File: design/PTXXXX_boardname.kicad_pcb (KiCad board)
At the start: 2 copper layers, 0 parts

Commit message: place some dummy parts for 1.0 1A release
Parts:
- added REF**: CP_Elec_3x5.3, Capacitor_SMD:CP_Elec_3x5.3, F.Cu at (120.1, 79.5)
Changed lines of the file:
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@@
     (tracks 0)
     (zones 0)
-    (modules 0)
+    (modules 1)
     (nets 1)
   )
@@
     (uvia_drill 0.1)
   )
+  (module Capacitor_SMD:CP_Elec_3x5.3 (layer F.Cu)
+    (at 120.1 79.5)
+    (descr "SMT capacitor, aluminium electrolytic, 3x5.3, Cornell Dubilier Electronics ")
+    (tags "Capacitor Electrolytic")
+    (attr smd)
+    (fp_text reference REF** (at 0 -2.7) (layer F.SilkS)
+      (effects (font (size 1 1) (thickness 0.15)))
+    )
+    (fp_text value CP_Elec_3x5.3 (at 0 2.7) (layer F.Fab)
+      (effects (font (size 1 1) (thickness 0.15)))
+    )
+    (fp_text user %R (at 0 0) (layer F.Fab)
+      (effects (font (size 0.6 0.6) (thickness 0.09)))
+    )
+    (fp_line (start -2.85 1.05) (end -1.78 1.05) (layer F.CrtYd) (width 0.05))
+    (fp_line (start -2.85 -1.05) (end -2.85 1.05) (layer F.CrtYd) (width 0.05))
+    (fp_line (start -1.78 -1.05) (end -2.85 -1.05) (layer F.CrtYd) (width 0.05))
+    (fp_line (start -1.78 -1.05) (end -0.93 -1.9) (layer F.CrtYd) (width 0.05))
+    (fp_line (start -1.78 1.05) (end -0.93 1.9) (layer F.CrtYd) (width 0.05))
+    (fp_line (start -0.93 -1.9) (end 1.9 -1.9) (layer F.CrtYd) (width 0.05))
+    (fp_line (start -0.93 1.9) (end 1.9 1.9) (layer F.CrtYd) (width 0.05))
+    (fp_line (start 1.9 1.05) (end 1.9 1.9) (layer F.CrtYd) (width 0.05))
+    (fp_line (start 2.85 1.05) (end 1.9 1.05) (layer F.CrtYd) (width 0.05))
+    (fp_line (start 2.85 -1.05) (end 2.85 1.05) (layer F.CrtYd) (width 0.05))
+    (fp_line (start 1.9 -1.05) (end 2.85 -1.05) (layer F.CrtYd) (width 0.05))
+    (fp_line (start 1.9 -1.9) (end 1.9 -1.05) (layer F.CrtYd) (width 0.05))
+    (fp_line (start -2.1875 -1.6225) (end -2.1875 -1.2475) (layer F.SilkS) (width 0.12))
+    (fp_line (start -2.375 -1.435) (end -2 -1.435) (layer F.SilkS) (width 0.12))
+    (fp_line (start -1.570563 1.06) (end -0.870563 1.76) (layer F.SilkS) (width 0.12))
+    (fp_line (start -1.570563 -1.06) (end -0.870563 -1.76) (layer F.SilkS) (width 0.12))
+    (fp_line (start -0.870563 1.76) (end 1.76 1.76) (layer F.SilkS) (width 0.12))
+    (fp_line (start -0.870563 -1.76) (end 1.76 -1.76) (layer F.SilkS) (width 0.12))
+    (fp_line (start 1.76 -1.76) (end 1.76 -1.06) (layer F.SilkS) (width 0.12))
+    (fp_line (start 1.76 1.76) (end 1.76 1.06) (layer F.SilkS) (width 0.12))
+    (fp_line (start -0.960469 -0.95) (end -0.960469 -0.65) (layer F.Fab) (width 0.1))
+    (fp_line (start -1.110469 -0.8) (end -0.810469 -0.8) (layer F.Fab) (width 0.1))
+    (fp_line (start -1.65 0.825) (end -0.825 1.65) (layer F.Fab) (width 0.1))
+    (fp_line (start -1.65 -0.825) (end -0.825 -1.65) (layer F.Fab) (width 0.1))
+    (fp_line (start -1.65 -0.825) (end -1.65 0.825) (layer F.Fab) (width 0.1))
+    (fp_line (start -0.825 1.65) (end 1.65 1.65) (layer F.Fab) (width 0.1))
+    (fp_line (start -0.825 -1.65) (end 1.65 -1.65) (layer F.Fab) (width 0.1))
+    (fp_line (start 1.65 -1.65) (end 1.65 1.65) (layer F.Fab) (width 0.1))
+    (fp_circle (center 0 0) (end 1.5 0) (layer F.Fab) (width 0.1))
+    (pad 2 smd rect (at 1.5 0) (size 2.2 1.6) (layers F.Cu F.Paste F.Mask))
+    (pad 1 smd rect (at -1.5 0) (size 2.2 1.6) (layers F.Cu F.Paste F.Mask))
+    (model ${KISYS3DMOD}/Capacitor_SMD.3dshapes/CP_Elec_3x5.3.wrl
+      (at (xyz 0 0 0))
+      (scale (xyz 1 1 1))
+      (rotate (xyz 0 0 0))
+    )
+  )
 )

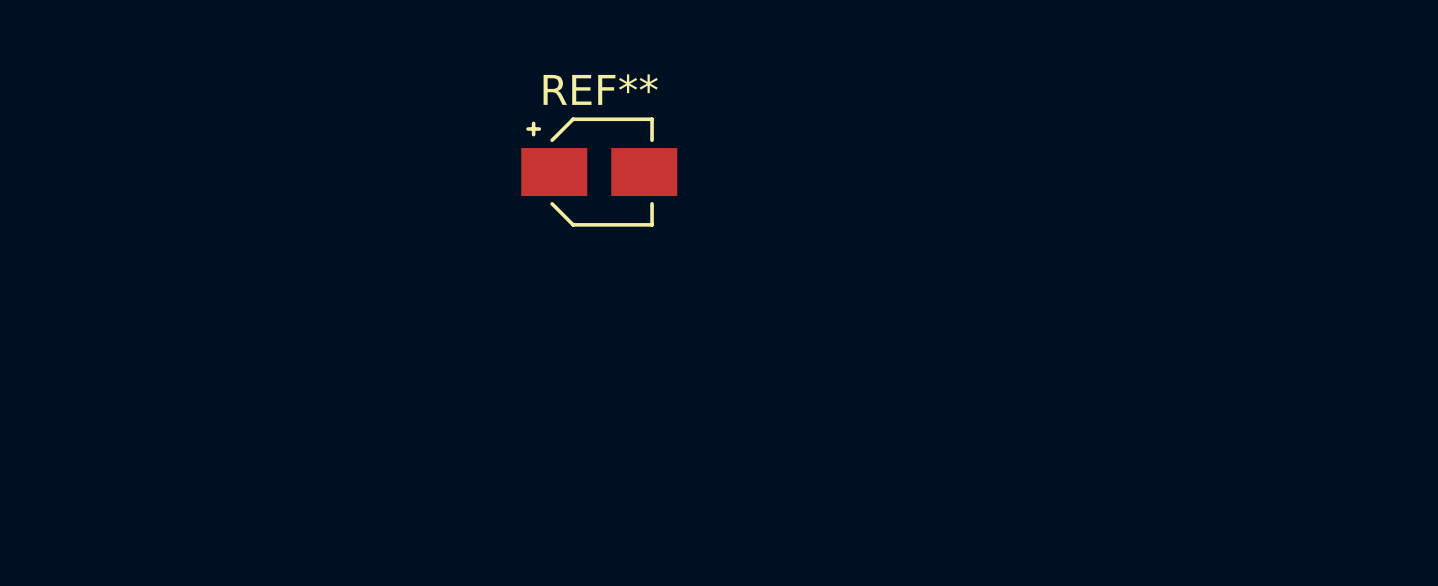
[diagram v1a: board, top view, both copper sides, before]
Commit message: test silk change to layout only for 1.1 1A release
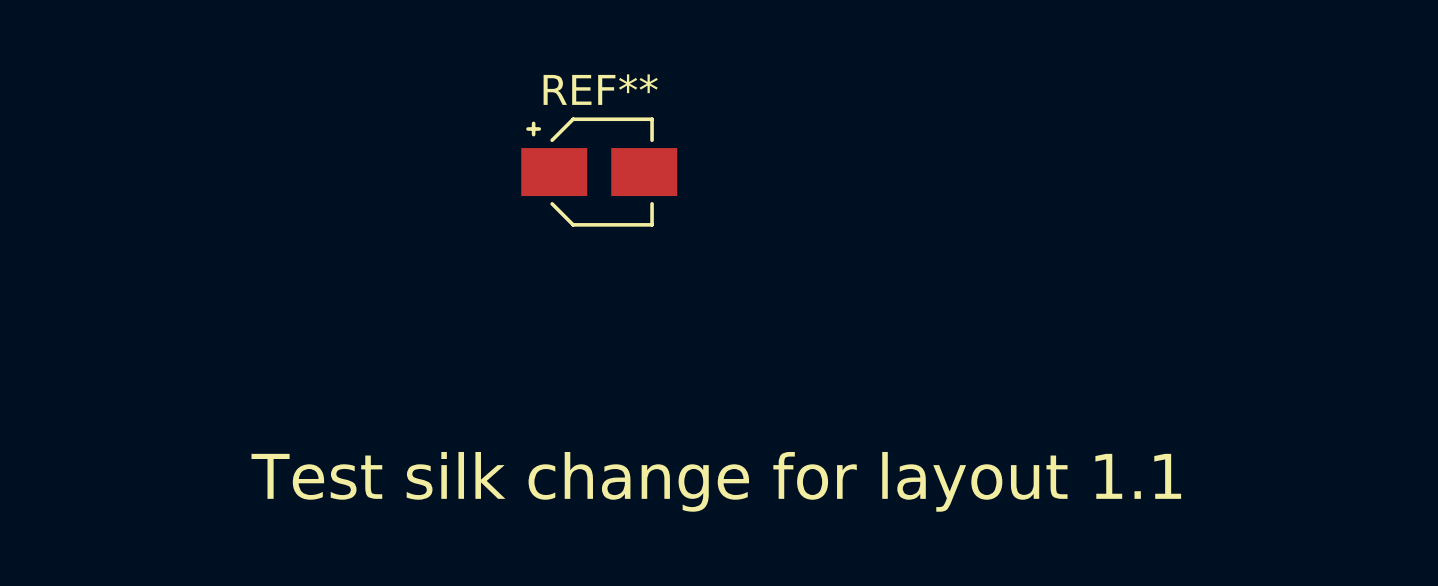
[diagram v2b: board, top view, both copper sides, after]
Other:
- board text added: "Test silk change for layout 1.1"
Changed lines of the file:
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@@
   (general
     (thickness 1.6)
-    (drawings 0)
+    (drawings 1)
     (tracks 0)
     (zones 0)
@@
     )
   )
+  (gr_text "Test silk change for layout 1.1" (at 124.1 89.7) (layer F.SilkS)
+    (effects (font (size 1.5 1.5) (thickness 0.3)))
+  )
 )
